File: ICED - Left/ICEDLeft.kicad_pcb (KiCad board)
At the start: 2 copper layers, 175.4 x 145.5 mm, 162 parts, among them P1 FLASH_HDR, P2 USB3_MICRO, P3 CONN_17, P4 USB3_AFEMALE, Q1 TC1264, U1 MK20DX256VLH7, U2 IS31FL3731C, X1 CRYSTAL

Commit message: ICED 1.2b, now with 100% more Type C
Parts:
- added R14: 5.1k, prettylib:SMD-1005, F.Cu at (108.6, 36.4)
- added R15: 5.1k, prettylib:SMD-1005, F.Cu at (113.2, 36.4)
- P2: value USB3_MICRO -> USBC; footprint prettylib:USB3_MICROB_STAKES -> prettylib:USB_C_MIDMOUNT_TH_IMPCUT
- R1, R2: moved to B.Cu
- moved R2 83.3 mm to (144.7, 110.2), turned to 180 degrees
- moved R1 82.3 mm to (143.4, 110.2), turned to 180 degrees
- moved C17 14.5 mm to (26.4, 41.0), turned to 0 degrees
- moved C16 12.6 mm to (27.9, 41.0), turned to 0 degrees
- moved C15 10.7 mm to (29.5, 41.0), turned to 0 degrees
- moved C14 8.80 mm to (31.0, 41.0), turned to 0 degrees
- moved P2 7.43 mm to (111.0, 32.5)
- moved C13 6.96 mm to (32.5, 41.0), turned to 0 degrees
- moved C4 0.54 mm to (141.9, 111.9)
- moved R10 0.51 mm to (52.8, 41.0)
- moved R13 0.51 mm to (24.3, 41.0)
- moved R9 0.51 mm to (55.8, 41.0)
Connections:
- net /mcu/PTB18 renamed /Col3
- net /mcu/PTB19 renamed /Col4
- net /mcu/PTB2 renamed /Col1
- net /mcu/PTB3 renamed /Col2
- net /mcu/PTC0 renamed /Col5
- net /mcu/PTC10 renamed /Col7
- net /mcu/PTC11 renamed /Col8
- net /mcu/PTC9 renamed /Col6
- net /mcu/PTD0 renamed /Col9
- net /mcu/PTD1 renamed /Row1
- net /mcu/PTD4 renamed /Row2
- net /mcu/PTD5 renamed /Row3
- net /mcu/PTD6 renamed /Row4
- net /mcu/PTD7 renamed /Row5
- P2 pad 1: +5V -> VSS
- P2 pad 10: (no net) -> /mcu/RX1
- P2 pad 11: /mcu/GND -> /mcu/TX1
- P2 pad 2: Net-(P2-Pad2) -> /mcu/TX1
- P2 pad 3: Net-(P2-Pad3) -> /mcu/RX1
- P2 pad 4: (no net) -> +5V
- P2 pad 5: VSS -> Net-(P2-Pad5)
- P2 pad 6: /mcu/RX1 -> /mcu/USB_DP
- P2 pad 7: /mcu/TX1 -> /mcu/USB_DM
- P2 pad 8: (no net) -> Net-(P2-Pad8)
- P2 pad 9: (no net) -> +5V
- P4 pad 10: /mcu/GND -> /GND
- P4 pad 2: (no net) -> Net-(P4-Pad2)
- P4 pad 3: (no net) -> Net-(P4-Pad3)
- P4 pad 7: (no net) -> Net-(P4-Pad7)
- P4 pad 8: (no net) -> Net-(P4-Pad8)
- P4 pad 9: (no net) -> Net-(P4-Pad9)
- R1 pad 1: Net-(P2-Pad2) -> /mcu/USB_DP
- R1 pad 2: /mcu/USB_DM -> Net-(R1-Pad2)
- R2 pad 1: Net-(P2-Pad3) -> /mcu/USB_DM
- R2 pad 2: /mcu/USB_DP -> Net-(R2-Pad2)
- S39 pad 1: (no net) -> Net-(S39-Pad1)
- U1 pad 10: (no net) -> /mcu/ADC0_DM0
- U1 pad 11: (no net) -> /mcu/ADC1_DP0
- U1 pad 12: (no net) -> /mcu/ADC1_DM0
- U1 pad 13: (no net) -> Net-(U1-Pad13)
- U1 pad 14: (no net) -> Net-(U1-Pad14)
- U1 pad 15: (no net) -> Net-(U1-Pad15)
- U1 pad 16: (no net) -> Net-(U1-Pad16)
- U1 pad 17: (no net) -> Net-(U1-Pad17)
- U1 pad 18: (no net) -> Net-(U1-Pad18)
- U1 pad 19: (no net) -> Net-(U1-Pad19)
- U1 pad 20: (no net) -> Net-(U1-Pad20)
- U1 pad 26: (no net) -> /mcu/PTA4
- U1 pad 28: (no net) -> /mcu/PTA12
- U1 pad 29: (no net) -> /mcu/PTA13
- U1 pad 5: /mcu/USB_DP -> Net-(R1-Pad2)
- U1 pad 6: /mcu/USB_DM -> Net-(R2-Pad2)
- U1 pad 9: (no net) -> /mcu/ADC0_DP0
- U2 pad 10: (no net) -> /mcu/CB4
- U2 pad 11: (no net) -> /mcu/CB5
- U2 pad 12: (no net) -> /mcu/CB6
- U2 pad 13: (no net) -> /mcu/CB7
- U2 pad 14: (no net) -> /mcu/CB8
- U2 pad 15: (no net) -> /mcu/CB9
- U2 pad 7: (no net) -> /mcu/CB1
- U2 pad 8: (no net) -> /mcu/CB2
- U2 pad 9: (no net) -> /mcu/CB3
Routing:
- net +5V: track 292.8 -> 218.9 mm, vias 2 -> 3
- net /mcu/GND: track 51.4 -> 0.00 mm
- net /GND: track 0.00 -> 45.5 mm
- net /mcu/SCL0: track 101.5 -> 72.1 mm, vias 1 -> 4
- net /ledmatrix/CA3: track 368.4 -> 389.0 mm
- net /ledmatrix/CA1: track 357.0 -> 376.8 mm
- net VSS: track 419.3 -> 399.5 mm, vias 8 -> 14
- net /mcu/SWD_DIO: track 72.4 -> 91.7 mm
- net /ledmatrix/CA4: track 273.0 -> 288.6 mm
- net /mcu/LCD_KR: track 159.9 -> 174.0 mm
- net /ledmatrix/CA2: track 418.0 -> 431.6 mm
- net Net-(C17-Pad2): track 15.4 -> 3.08 mm
- net /ledmatrix/CA5: track 297.7 -> 309.3 mm
- net /mcu/RX0: track 182.1 -> 171.1 mm, vias 4 -> 2
- net Net-(C16-Pad2): track 13.4 -> 3.08 mm
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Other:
- board size 175.4 x 145.5 mm -> 175.4 x 145 mm
- net class 4mil added: clearance 0.1016, trace_width 0.1016, via_dia 0.4064, via_drill 0.2032
- net class Default: clearance 0.1524 -> 0.1016; via_dia 0.6096 -> 0.4064; via_drill 0.3048 -> 0.2032
- net class GND: clearance 0.1524 -> 0.1016
- net class Power: clearance 0.1524 -> 0.1016
- rule pad_to_mask_clearance: 0.0762 -> 0.0508
- rule trace_clearance: 0.1524 -> 0.1016
- rule via_min_drill: 0.3048 -> 0.2032
- rule via_min_size: 0.508 -> 0.4064
- board text added: "ICED-L Rev 1.2b Batch __"
- board text removed: "ICED-L Rev 1.1d Batch __"

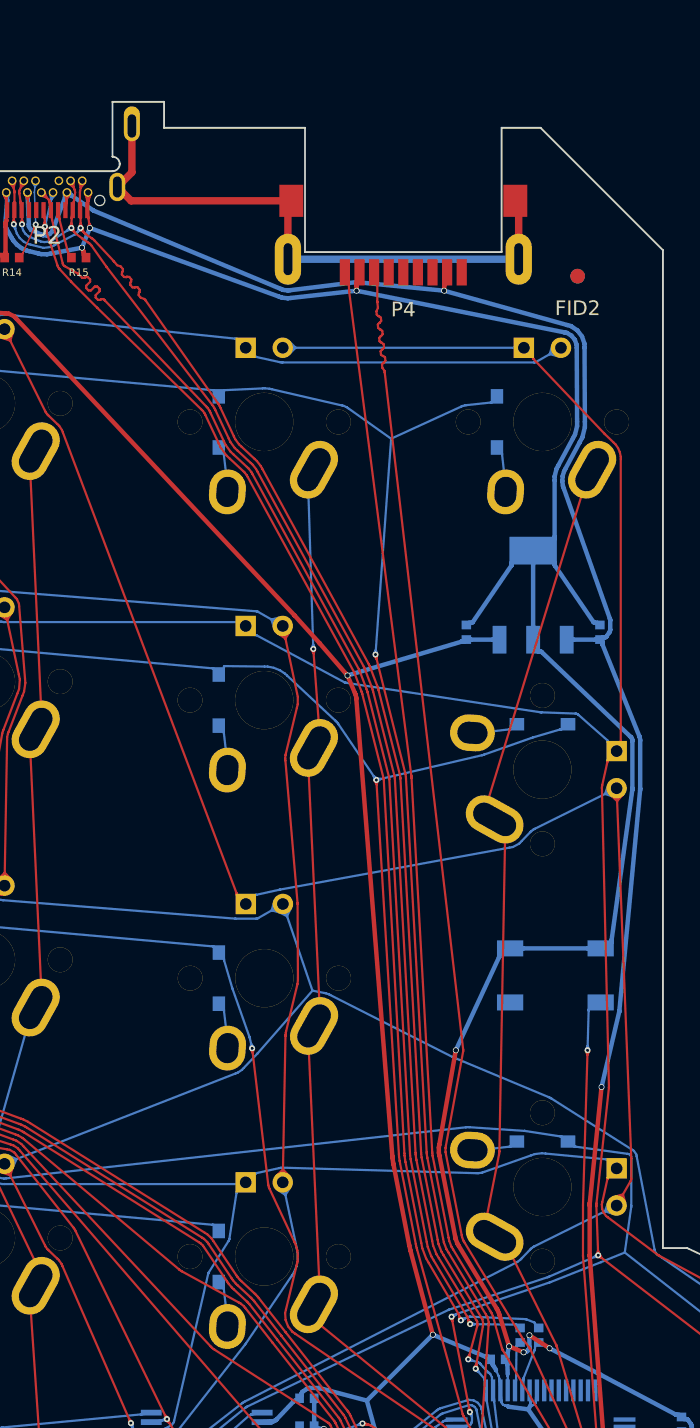
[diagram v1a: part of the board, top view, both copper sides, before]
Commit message: Update the left USB A connector
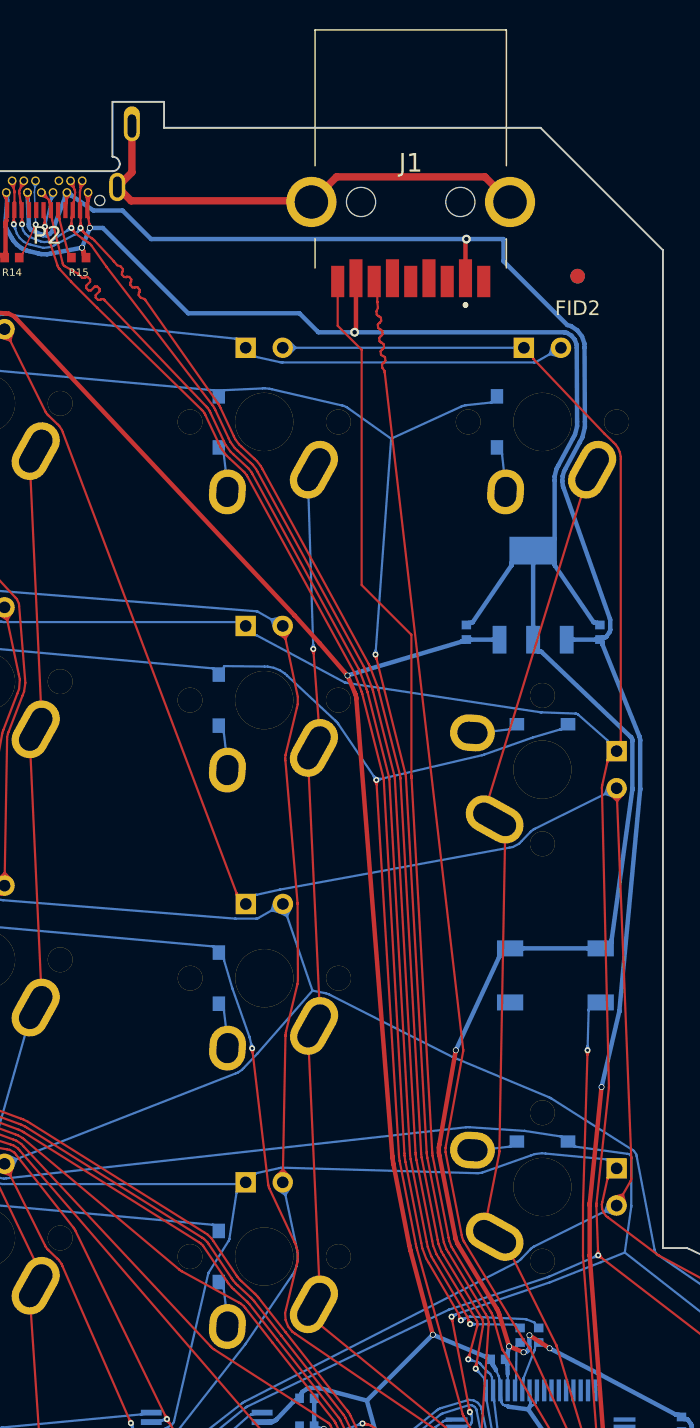
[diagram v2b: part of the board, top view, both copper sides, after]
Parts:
- removed P4: USB3_AFEMALE, prettylib:USB3_AFEMALE_MOD
- added J1: 692122030100, prettylib:692122030100, F.Cu at (135.9, 32.6)
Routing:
- net /GND: track 45.5 -> 38.0 mm
- net VSS: track 399.5 -> 403.8 mm
- net +5V: track 218.9 -> 222.9 mm
- net /mcu/TX0: track 177.4 -> 178.6 mm
- net /mcu/RX0: track 171.1 -> 170.6 mm
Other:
- outline, holes or cut-outs redrawn
